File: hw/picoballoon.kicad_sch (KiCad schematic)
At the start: 27 parts, among them J1 Conn_ARM_JTAG_SWD_10, J4 u.fl, U1 TPS610994YFFR, U2 K32L2B21VLH0A, U3 L96-M33, U4 INNOCOMM-SN10-11, U5 MS561101BA03-50

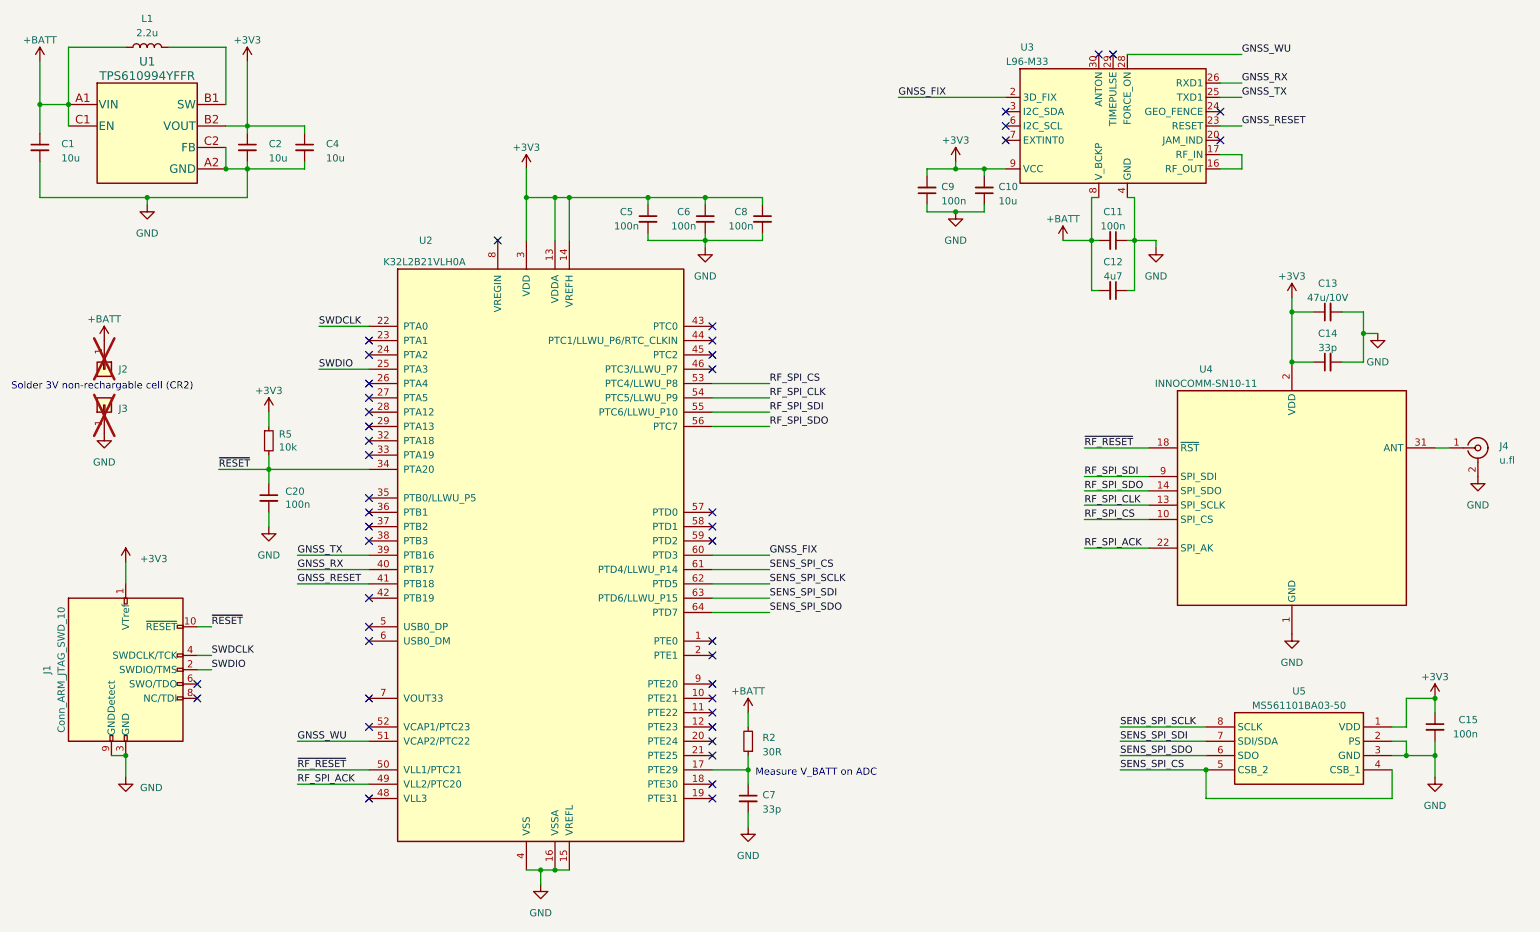
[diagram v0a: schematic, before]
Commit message: change gps reset pin
cleanup pcb tracks
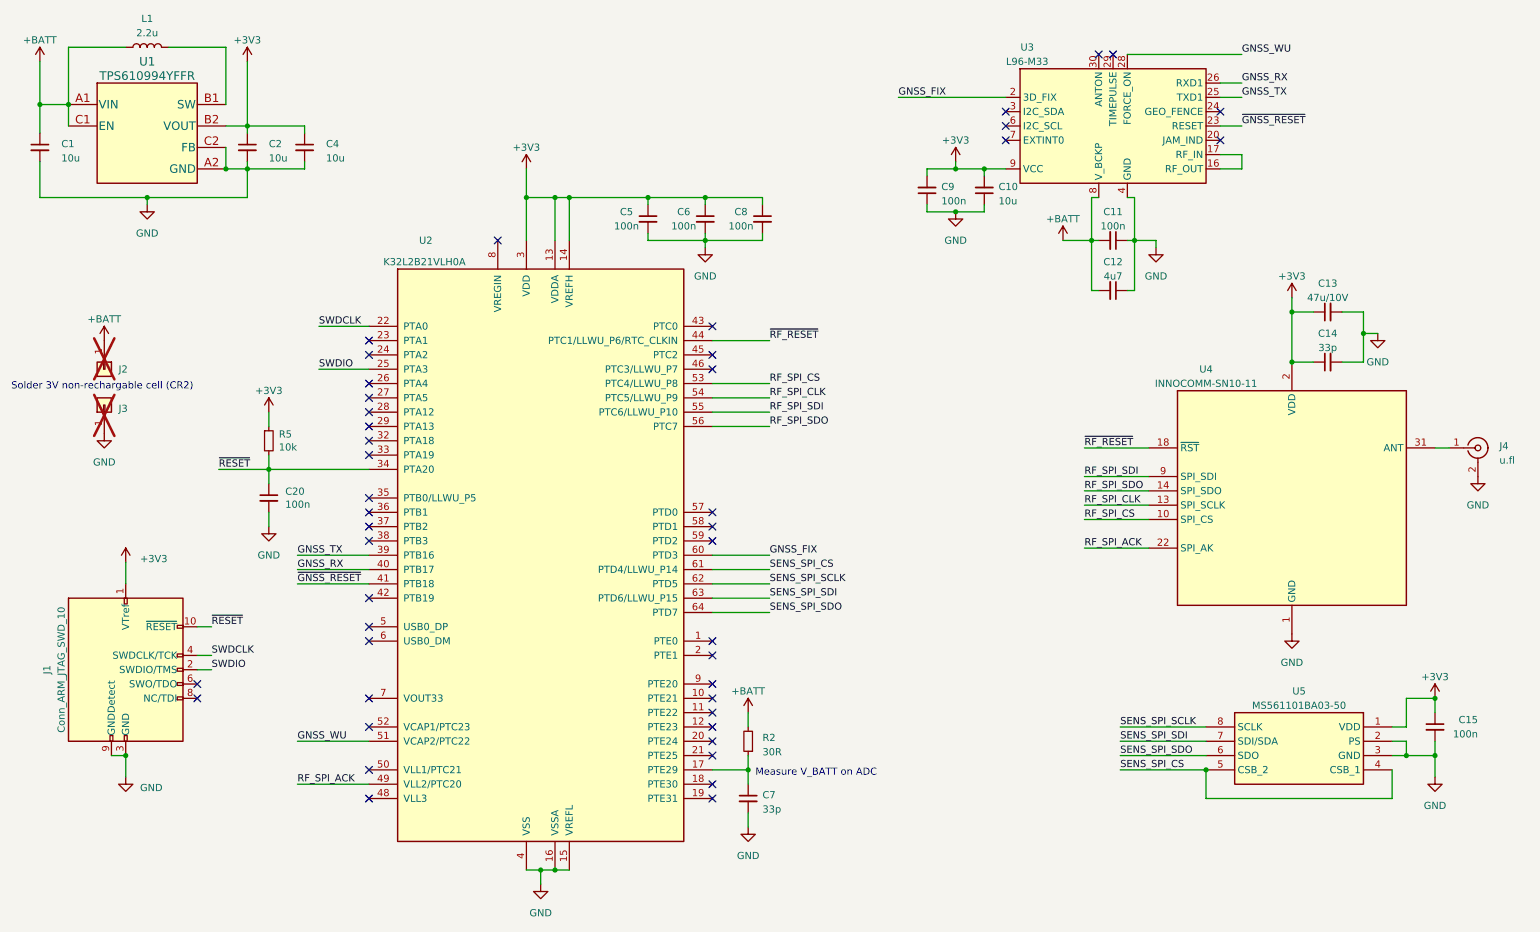
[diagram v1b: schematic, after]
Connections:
- net ~{RF_RESET}: now also U2.44 (PTC1/LLWU_P6/RTC_CLKIN); no longer U2.50 (VLL1/PTC21)
- net GNSS_RESET renamed ~{GNSS_RESET}
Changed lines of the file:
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@@
   (no_connect (at 77.47 91.44))
   (no_connect (at 77.47 101.6))
-  (no_connect (at 138.43 73.66))
   (no_connect (at 138.43 127))
   (no_connect (at 209.55 22.86))
@@
   (no_connect (at 77.47 73.66))
   (no_connect (at 138.43 144.78))
+  (no_connect (at 77.47 149.86))
   (no_connect (at 138.43 142.24))
   (no_connect (at 77.47 124.46))
@@
     (stroke (width 0) (type default))
   )
+  (wire (pts (xy 138.43 73.66) (xy 148.59 73.66))
+    (stroke (width 0) (type default))
+  )
   (wire (pts (xy 259.08 149.86) (xy 259.08 154.94))
     (stroke (width 0) (type default))
@@
     (stroke (width 0) (type default))
   )
-  (wire (pts (xy 64.77 149.86) (xy 77.47 149.86))
-    (stroke (width 0) (type default))
-  )
   (wire (pts (xy 46.99 124.46) (xy 49.53 124.46))
     (stroke (width 0) (type default))
@@
     (effects (font (size 1.27 1.27)) (justify left bottom))
   )
+  (label "~{RF_RESET}" (at 148.59 73.66 0) (fields_autoplaced)
+    (effects (font (size 1.27 1.27)) (justify left bottom))
+  )
   (label "~{RESET}" (at 50.8 96.52 0) (fields_autoplaced)
     (effects (font (size 1.27 1.27)) (justify left bottom))
@@
     (effects (font (size 1.27 1.27)) (justify left bottom))
   )
-  (label "GNSS_RESET" (at 232.41 35.56 0) (fields_autoplaced)
+  (label "~{GNSS_RESET}" (at 232.41 35.56 0) (fields_autoplaced)
     (effects (font (size 1.27 1.27)) (justify left bottom))
   )
@@
     (effects (font (size 1.27 1.27)) (justify left bottom))
   )
-  (label "~{RF_RESET}" (at 64.77 149.86 0) (fields_autoplaced)
-    (effects (font (size 1.27 1.27)) (justify left bottom))
-  )
   (label "SWDCLK" (at 49.53 129.54 0) (fields_autoplaced)
     (effects (font (size 1.27 1.27)) (justify left bottom))
@@
     (effects (font (size 1.27 1.27)) (justify left bottom))
   )
-  (label "GNSS_RESET" (at 64.77 116.84 0) (fields_autoplaced)
-    (effects (font (size 1.27 1.27)) (justify left bottom))
-  )
+  (label "~{GNSS_RESET}" (at 64.77 116.84 0) (fields_autoplaced)
+    (effects (font (size 1.27 1.27)) (justify left bottom))
+  )

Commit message: fix swd footprint
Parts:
- J1: footprint Connector_PinSocket_1.27mm:PinSocket_2x05_P1.27mm_Vertical -> Connector_PinHeader_1.27mm:PinHeader_2x05_P1.27mm_Vertical
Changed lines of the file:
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@@
       (effects (font (size 1.27 1.27)))
     )
-    (property "Footprint" "Connector_PinSocket_1.27mm:PinSocket_2x05_P1.27mm_Vertical" (at 34.29 132.08 0)
+    (property "Footprint" "Connector_PinHeader_1.27mm:PinHeader_2x05_P1.27mm_Vertical" (at 34.29 132.08 0)
       (effects (font (size 1.27 1.27)) hide)
     )
